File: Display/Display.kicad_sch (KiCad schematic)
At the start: 1 part, among them U1 74HC595

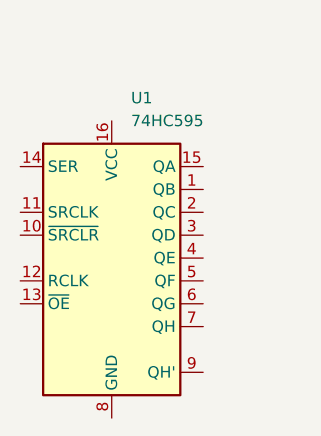
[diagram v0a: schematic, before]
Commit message: detach shift register
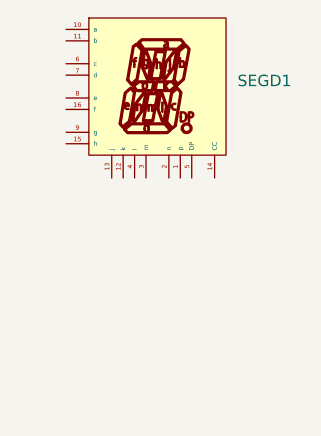
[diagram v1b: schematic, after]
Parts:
- removed U1: 74HC595, Package_SO:TSSOP-16_4.4x5mm_P0.65mm, symbol 74xx:74HC595
- added SEGD1: (no value), External_Parts:ACPSC04-41SEKWA, symbol External_Parts:ACPSC04-41SEKWA
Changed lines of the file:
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@@
 	(paper "A4")
 	(symbol
-		(lib_id "74xx:74HC595")
-		(at 82.55 72.39 0)
+		(lib_id "External_Parts:ACPSC04-41SEKWA")
+		(at 87.63 53.34 0)
 		(unit 1)
 		(exclude_from_sim no)
@@
 		(dnp no)
 		(fields_autoplaced yes)
-		(property "Reference" "U1"
-			(at 84.6933 54.61 0)
+		(property "Reference" "SEGD1"
+			(at 96.52 52.7049 0)
 			(effects
 				(font
@@
 			)
 		)
-		(property "Value" "74HC595"
-			(at 84.6933 57.15 0)
+		(property "Value" ""
+			(at 96.52 54.61 0)
 			(effects
 				(font
@@
 			)
 		)
-		(property "Footprint" "Package_SO:TSSOP-16_4.4x5mm_P0.65mm"
-			(at 82.55 72.39 0)
+		(property "Footprint" "External_Parts:ACPSC04-41SEKWA"
+			(at 87.63 53.34 0)
 			(effects
 				(font
@@
 			)
 		)
-		(property "Datasheet" "http://www.ti.com/lit/ds/symlink/sn74hc595.pdf"
-			(at 82.55 72.39 0)
+		(property "Datasheet" ""
+			(at 87.63 53.34 0)
 			(effects
 				(font
@@
 			)
 		)
-		(property "Description" "8-bit serial in/out Shift Register 3-State Outputs"
-			(at 82.55 72.39 0)
+		(property "Description" ""
+			(at 87.63 53.34 0)
 			(effects
 				(font
@@
 			)
 		)
-		(pin "14"
+		(pin "10"
+		)
+		(pin "11"
+		)
+		(pin "6"
+		)
+		(pin "7"
+		)
+		(pin "8"
+		)
+		(pin "16"
+		)
+		(pin "9"
+		)
+		(pin "15"
 		)
 		(pin "13"
-		)
-		(pin "10"
 		)
 		(pin "12"
@@
 		(pin "4"
 		)
-		(pin "5"
+		(pin "3"
 		)
-		(pin "6"
-		)
-		(pin "16"
-		)
-		(pin "11"
-		)
-		(pin "15"
+		(pin "2"
 		)
 		(pin "1"
 		)
-		(pin "2"
+		(pin "5"
 		)
-		(pin "3"
-		)
-		(pin "8"
-		)
-		(pin "7"
-		)
-		(pin "9"
+		(pin "14"
 		)
 		(instances
 			(project ""
 				(path "/4a3e89f9-ab44-4b68-b8a8-f6bfa5391fb1"
-					(reference "U1")
+					(reference "SEGD1")
 					(unit 1)
 				)

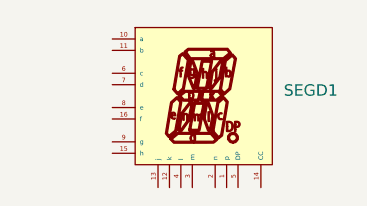
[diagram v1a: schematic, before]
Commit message: add chosen resistor
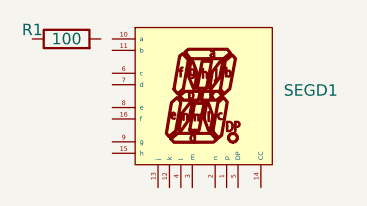
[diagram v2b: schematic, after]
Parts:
- added R1: 100, Resistor_SMD:R_0402_1005Metric_Pad0.72x0.64mm_HandSolder, symbol Device:R
- SEGD1: value (none) -> ~
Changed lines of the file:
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@@
 			)
 		)
-		(property "Value" ""
+		(property "Value" "~"
 			(at 96.52 54.61 0)
 			(effects
@@
 					(unit 1)
 				)
+			)
+		)
+	)
+	(symbol
+		(lib_id "Device:R")
+		(at 72.39 46.99 90)
+		(unit 1)
+		(exclude_from_sim no)
+		(in_bom yes)
+		(on_board yes)
+		(dnp no)
+		(property "Reference" "R1"
+			(at 68.58 45.974 90)
+			(effects
+				(font
+					(size 1.27 1.27)
+				)
+			)
+		)
+		(property "Value" "100"
+			(at 72.39 46.99 90)
+			(effects
+				(font
+					(size 1.27 1.27)
+				)
+			)
+		)
+		(property "Footprint" "Resistor_SMD:R_0402_1005Metric_Pad0.72x0.64mm_HandSolder"
+			(at 72.39 48.768 90)
+			(effects
+				(font
+					(size 1.27 1.27)
+				)
+				(hide yes)
+			)
+		)
+		(property "Datasheet" "https://jlcpcb.com/api/file/downloadByFileSystemAccessId/8579705907481001984"
+			(at 72.39 46.99 0)
+			(effects
+				(font
+					(size 1.27 1.27)
+				)
+				(hide yes)
+			)
+		)
+		(property "Description" "Resistor"
+			(at 72.39 46.99 0)
+			(effects
+				(font
+					(size 1.27 1.27)
+				)
+				(hide yes)
+			)
+		)
+		(property "LCSC" "C25076"
+			(at 72.39 46.99 90)
+			(effects
+				(font
+					(size 1.27 1.27)
+				)
+				(hide yes)
+			)
+		)
+		(pin "2"
+		)
+		(pin "1"
+		)
+		(instances
+			(project ""
+				(path "/4a3e89f9-ab44-4b68-b8a8-f6bfa5391fb1"
+					(reference "R1")
+					(unit 1)
+				)

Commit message: user save
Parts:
- added R10, R100, R101, R102, R103, R104, R105, R106, R107, R108, R109, R11, R110, R111, R112, R113, R114, R115, R116, R117, R118, R119, R12, R120, R121, R122, R123, R124, R125, R126, R127, R128, R129, R13, R130, R131, R132, R133, R134, R135, R136, R137, R138, R139, R14, R140, R141, R142, R143, R144, R145, R146, R147, R148, R149, R15, R150, R151, R152, R153, R154, R155, R156, R157, R158, R159, R16, R160, R161, R162, R163, R164, R165, R166, R167, R168, R169, R17, R170, R171, R172, R173, R174, R175, R176, R177, R178, R179, R18, R180, R181, R182, R183, R184, R185, R186, R187, R188, R189, R19, R190, R191, R192, R193, R194, R195, R196, R197, R198, R199, R2, R20, R200, R201, R202, R203, R204, R205, R206, R207, R208, R209, R21, R210, R211, R212, R213, R214, R215, R216, R217, R218, R219, R22, R220, R221, R222, R223, R224, R225, R226, R227, R228, R229, R23, R230, R231, R232, R233, R234, R235, R236, R237, R238, R239, R24, R240, R241, R242, R243, R244, R245, R246, R247, R248, R249, R25, R250, R251, R252, R253, R254, R255, R256, R257, R258, R259, R26, R260, R261, R262, R263, R264, R265, R266, R267, R268, R269, R27, R270, R271, R272, R273, R274, R275, R276, R277, R278, R279, R28, R280, R281, R282, R283, R284, R285, R286, R287, R288, R289, R29, R290, R291, R292, R293, R294, R295, R296, R297, R298, R299, R3, R30, R300, R301, R302, R303, R304, R305, R306, R307, R308, R309, R31, R310, R311, R312, R313, R314, R315, R316, R317, R318, R319, R32, R320, R321, R322, R323, R324, R325, R326, R327, R328, R329, R33, R330, R331, R332, R333, R334, R335, R336, R337, R338, R339, R34, R340, R341, R342, R343, R344, R345, R346, R347, R348, R349, R35, R350, R351, R352, R353, R354, R355, R356, R357, R358, R359, R36, R360, R361, R362, R363, R364, R365, R366, R367, R368, R369, R37, R370, R371, R372, R373, R374, R375, R376, R377, R378, R379, R38, R380, R381, R382, R383, R384, R385, R386, R387, R388, R389, R39, R390, R391, R392, R393, R394, R395, R396, R397, R398, R399, R4, R40, R400, R401, R402, R403, R404, R405, R406, R407, R408, R409, R41, R410, R411, R412, R413, R414, R415, R416, R417, R418, R419, R42, R420, R421, R422, R423, R424, R425, R426, R427, R428, R429, R43, R430, R431, R432, R433, R434, R435, R436, R437, R438, R439, R44, R440, R441, R442, R443, R444, R445, R446, R447, R448, R449, R45, R450, R451, R452, R453, R454, R455, R456, R457, R458, R459, R46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: 100, Resistor_SMD:R_0402_1005Metric_Pad0.72x0.64mm_HandSolder, symbol Device:R
- added SEGD2, SEGD3, SEGD4, SEGD5: ~, External_Parts:ACPSC04-41SEKWA, symbol External_Parts:ACPSC04-41SEKWA
- added U1, U10, U11, U12, U13, U14, U15, U16, U17, U18, U19, U2, U20, U21, U22, U23, U24, U25, U26, U27, U28, U29, U3, U30, U31, U32, U33, U34, U35, U36, U37, U38, U39, U4, U40, U41, U42, U43, U44, U45, U46, U47, U48, U49, U5, U50, U51, U52, U53, U54, U55, U56, U57, U58, U59, U6, U60, U61, U62, U63, U64, U65, U66, U67, U68, U69, U7, U70, U8, U9: 74HC595, Package_SO:TSSOP-16_4.4x5mm_P0.65mm, symbol 74xx:74HC595
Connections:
- net at SEGD1.1 (p): now also R14.2
- net at SEGD1.10 (a): now also R1.2
- net at SEGD1.11 (b): now also R2.2
- net at SEGD1.12 (k): now also R10.2
- net at SEGD1.13 (j): now also R9.2
- net GNDD: now reaches SEGD1.14 (CC)
- net GNDD: now also SEGD2.14 (CC), SEGD3.14 (CC), SEGD4.14 (CC), SEGD5.14 (CC), U1.8 (GND), U10.8 (GND), U11.8 (GND), U12.8 (GND), U13.8 (GND), U14.8 (GND), U15.8 (GND), U16.8 (GND)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
- net at SEGD1.15 (h): now also R8.2
- net at SEGD1.16 (f): now also R6.2
- net at SEGD1.2 (n): now also R13.2
- net at SEGD1.3 (m): now also R12.2
- net at SEGD1.4 (l): now also R11.2
- net at SEGD1.5 (DP): now also R15.2
- net at SEGD1.6 (c): now also R3.2
- net at SEGD1.7 (d): now also R4.2
- net at SEGD1.8 (e): now also R5.2
- net at SEGD1.9 (g): now also R7.2
- net at R1.1: now also U1.15 (QA)
- new net: R72.1, U9.7 (QH)
- new net: R72.2, SEGD5.3 (m)
- new net: R126.1, U16.5 (QF)
- new net: R34.1, U5.1 (QB)
- new net: R33.1, U5.15 (QA)
- new net: R35.1, U5.2 (QC)
- new net: R36.1, U5.3 (QD)
- new net: R37.1, U5.4 (QE)
- new net: R38.1, U5.5 (QF)
- new net: R39.1, U5.6 (QG)
- new net: R40.1, U5.7 (QH)
- new net: R335.1, U42.6 (QG)
- new net: R112.1, U14.7 (QH)
- new net: R535.1, U67.6 (QG)
- new net: R282.1, U36.1 (QB)
- new net: R427.1, U54.2 (QC)
- new net: R174.1, U22.5 (QF)
- new net: R435.1, U55.2 (QC)
- new net: R527.1, U66.6 (QG)
- new net: R510.1, U64.5 (QF)
- new net: R76.1, U10.3 (QD)
- new net: R468.1, U59.3 (QD)
- new net: R178.1, U23.1 (QB)
- new net: R177.1, U23.15 (QA)
- new net: R179.1, U23.2 (QC)
- new net: R180.1, U23.3 (QD)
- new net: R181.1, U23.4 (QE)
- new net: R182.1, U23.5 (QF)
- new net: R183.1, U23.6 (QG)
- new net: R184.1, U23.7 (QH)
- new net: R474.1, U60.1 (QB)
- new net: R411.1, U52.2 (QC)
- new net: R59.1, U8.2 (QC)
- new net: R59.2, SEGD4.1 (p)
- new net: R461.1, U58.4 (QE)
- new net: R278.1, U35.5 (QF)
- new net: R194.1, U25.1 (QB)
- new net: R193.1, U25.15 (QA)
- new net: R195.1, U25.2 (QC)
- new net: R196.1, U25.3 (QD)
- new net: R197.1, U25.4 (QE)
- new net: R198.1, U25.5 (QF)
- new net: R199.1, U25.6 (QG)
- new net: R200.1, U25.7 (QH)
- new net: R397.1, U50.4 (QE)
- new net: R145.1, U19.15 (QA)
- new net: R300.1, U38.3 (QD)
- new net: R516.1, U65.3 (QD)
- new net: R543.1, U68.6 (QG)
- new net: R323.1, U41.2 (QC)
- new net: R286.1, U36.5 (QF)
- new net: R66.1, U9.1 (QB)
- new net: R66.2, SEGD5.16 (f)
- new net: R489.1, U62.15 (QA)
- new net: R192.1, U24.7 (QH)
- new net: R449.1, U57.15 (QA)
- new net: R331.1, U42.2 (QC)
- new net: R86.1, U11.5 (QF)
- new net: R549.1, U69.4 (QE)
- new net: R167.1, U21.6 (QG)
- new net: R553.1, U70.15 (QA)
- new net: R529.1, U67.15 (QA)
- new net: R82.1, U11.1 (QB)
- new net: R318.1, U40.5 (QF)
- new net: R356.1, U45.3 (QD)
- new net: R437.1, U55.4 (QE)
- new net: R324.1, U41.3 (QD)
- new net: R490.1, U62.1 (QB)
- new net: R400.1, U50.7 (QH)
- new net: R154.1, U20.1 (QB)
- new net: R46.2, SEGD4.10 (a)
- new net: R47.2, SEGD4.11 (b)
- new net: R55.2, SEGD4.12 (k)
- new net: R54.2, SEGD4.13 (j)
- new net: R53.2, SEGD4.15 (h)
- new net: R51.2, SEGD4.16 (f)
- new net: R58.2, SEGD4.2 (n)
- new net: R57.2, SEGD4.3 (m)
- new net: R56.2, SEGD4.4 (l)
- new net: R60.2, SEGD4.5 (DP)
- new net: R48.2, SEGD4.6 (c)
- new net: R49.2, SEGD4.7 (d)
- new net: R50.2, SEGD4.8 (e)
- new net: R52.2, SEGD4.9 (g)
- new net: R98.1, U13.1 (QB)
- new net: R97.1, U13.15 (QA)
- new net: R99.1, U13.2 (QC)
- new net: R100.1, U13.3 (QD)
- new net: R101.1, U13.4 (QE)
- new net: R102.1, U13.5 (QF)
- new net: R103.1, U13.6 (QG)
- new net: R104.1, U13.7 (QH)
- new net: R311.1, U39.6 (QG)
- new net: R338.1, U43.1 (QB)
- new net: R506.1, U64.1 (QB)
- new net: R505.1, U64.15 (QA)
- new net: R507.1, U64.2 (QC)
- new net: R508.1, U64.3 (QD)
- new net: R509.1, U64.4 (QE)
- new net: R511.1, U64.6 (QG)
- new net: R512.1, U64.7 (QH)
- new net: R105.1, U14.15 (QA)
- new net: R367.1, U46.6 (QG)
- new net: R62.1, U8.5 (QF)
- new net: R62.2, SEGD5.11 (b)
- new net: R67.1, U9.2 (QC)
- new net: R67.2, SEGD5.9 (g)
- new net: R425.1, U54.15 (QA)
- new net: R550.1, U69.5 (QF)
- new net: R548.1, U69.3 (QD)
- new net: R519.1, U65.6 (QG)
- new net: R63.1, U8.6 (QG)
- new net: R63.2, SEGD5.6 (c)
- new net: R537.1, U68.15 (QA)
- new net: R348.1, U44.3 (QD)
- new net: R185.1, U24.15 (QA)
- new net: R269.1, U34.4 (QE)
- new net: R405.1, U51.4 (QE)
- new net: R117.1, U15.4 (QE)
- new net: R222.1, U28.5 (QF)
- new net: R423.1, U53.6 (QG)
- new net: R149.1, U19.4 (QE)
- new net: R551.1, U69.6 (QG)
- new net: R5.1, U1.4 (QE)
- new net: R131.1, U17.2 (QC)
- new net: R33.2, SEGD3.6 (c)
- new net: R221.1, U28.4 (QE)
- new net: R68.1, U9.3 (QD)
- new net: R68.2, SEGD5.15 (h)
- new net: R32.1, U4.7 (QH)
- new net: R32.2, SEGD3.11 (b)
- new net: R290.1, U37.1 (QB)
- new net: R254.1, U32.5 (QF)
- new net: R189.1, U24.4 (QE)
- new net: R339.1, U43.2 (QC)
- new net: R436.1, U55.3 (QD)
- new net: R471.1, U59.6 (QG)
- new net: R123.1, U16.2 (QC)
- new net: R283.1, U36.2 (QC)
- new net: R442.1, U56.1 (QB)
- new net: R299.1, U38.2 (QC)
- new net: R85.1, U11.4 (QE)
- new net: R233.1, U30.15 (QA)
- new net: R136.1, U17.7 (QH)
- new net: R354.1, U45.1 (QB)
- new net: R353.1, U45.15 (QA)
- new net: R355.1, U45.2 (QC)
- new net: R357.1, U45.4 (QE)
- new net: R358.1, U45.5 (QF)
- new net: R359.1, U45.6 (QG)
- new net: R360.1, U45.7 (QH)
- new net: R89.1, U12.15 (QA)
- new net: R94.1, U12.5 (QF)
- new net: R308.1, U39.3 (QD)
- new net: R457.1, U58.15 (QA)
- new net: R464.1, U58.7 (QH)
- new net: R499.1, U63.2 (QC)
- new net: R448.1, U56.7 (QH)
- new net: R191.1, U24.6 (QG)
- new net: R234.1, U30.1 (QB)
- new net: R113.1, U15.15 (QA)
- new net: R34.2, SEGD3.7 (d)
- new net: R284.1, U36.3 (QD)
- new net: R334.1, U42.5 (QF)
- new net: R110.1, U14.5 (QF)
- new net: R540.1, U68.3 (QD)
- new net: R202.1, U26.1 (QB)
- new net: R205.1, U26.4 (QE)
- new net: R71.1, U9.6 (QG)
- new net: R71.2, SEGD5.4 (l)
- new net: R394.1, U50.1 (QB)
- new net: R393.1, U50.15 (QA)
- new net: R395.1, U50.2 (QC)
- new net: R396.1, U50.3 (QD)
- new net: R398.1, U50.5 (QF)
- new net: R399.1, U50.6 (QG)
- new net: R559.1, U70.6 (QG)
- new net: R350.1, U44.5 (QF)
- new net: R230.1, U29.5 (QF)
- new net: R132.1, U17.3 (QD)
- new net: R143.1, U18.6 (QG)
- new net: R249.1, U32.15 (QA)
- new net: R115.1, U15.2 (QC)
- new net: R227.1, U29.2 (QC)
- new net: R554.1, U70.1 (QB)
- new net: R87.1, U11.6 (QG)
- new net: R558.1, U70.5 (QF)
- new net: R410.1, U52.1 (QB)
- new net: R250.1, U32.1 (QB)
- new net: R251.1, U32.2 (QC)
- new net: R252.1, U32.3 (QD)
- new net: R253.1, U32.4 (QE)
- new net: R255.1, U32.6 (QG)
- new net: R256.1, U32.7 (QH)
- new net: R50.1, U7.1 (QB)
- new net: R21.1, U3.4 (QE)
- new net: R21.2, SEGD2.16 (f)
- new net: R129.1, U17.15 (QA)
- new net: R153.1, U20.15 (QA)
- new net: R155.1, U20.2 (QC)
- new net: R156.1, U20.3 (QD)
- new net: R157.1, U20.4 (QE)
- new net: R158.1, U20.5 (QF)
- new net: R159.1, U20.6 (QG)
- new net: R160.1, U20.7 (QH)
- new net: R288.1, U36.7 (QH)
- new net: R469.1, U59.4 (QE)
- new net: R536.1, U67.7 (QH)
- new net: R201.1, U26.15 (QA)
- new net: R10.1, U2.1 (QB)
- new net: R170.1, U22.1 (QB)
- new net: R88.1, U11.7 (QH)
- new net: R7.1, U1.6 (QG)
- new net: R11.1, U2.2 (QC)
- new net: R210.1, U27.1 (QB)
- new net: R209.1, U27.15 (QA)
- new net: R211.1, U27.2 (QC)
- new net: R212.1, U27.3 (QD)
- new net: R213.1, U27.4 (QE)
- new net: R214.1, U27.5 (QF)
- new net: R215.1, U27.6 (QG)
- new net: R216.1, U27.7 (QH)
- new net: R362.1, U46.1 (QB)
- new net: R361.1, U46.15 (QA)
- new net: R363.1, U46.2 (QC)
- new net: R364.1, U46.3 (QD)
- new net: R365.1, U46.4 (QE)
- new net: R366.1, U46.5 (QF)
- new net: R368.1, U46.7 (QH)
- new net: R18.1, U3.1 (QB)
- new net: R17.1, U3.15 (QA)
- new net: R19.1, U3.2 (QC)
- new net: R20.1, U3.3 (QD)
- new net: R22.1, U3.5 (QF)
- new net: R23.1, U3.6 (QG)
- new net: R24.1, U3.7 (QH)
- new net: R138.1, U18.1 (QB)
- new net: R426.1, U54.1 (QB)
- new net: R428.1, U54.3 (QD)
- new net: R429.1, U54.4 (QE)
- new net: R430.1, U54.5 (QF)
- new net: R431.1, U54.6 (QG)
- new net: R432.1, U54.7 (QH)
- new net: R44.1, U6.3 (QD)
- new net: R44.2, SEGD3.1 (p)
- new net: R289.1, U37.15 (QA)
- new net: R139.1, U18.2 (QC)
- new net: R458.1, U58.1 (QB)
- new net: R459.1, U58.2 (QC)
- new net: R460.1, U58.3 (QD)
- new net: R462.1, U58.5 (QF)
- new net: R463.1, U58.6 (QG)
- new net: R203.1, U26.2 (QC)
- new net: R275.1, U35.2 (QC)
- new net: R75.1, U10.2 (QC)
- new net: R75.2, SEGD5.5 (DP)
- new net: R491.1, U62.2 (QC)
- new net: R492.1, U62.3 (QD)
- new net: R493.1, U62.4 (QE)
- new net: R494.1, U62.5 (QF)
- new net: R495.1, U62.6 (QG)
- new net: R496.1, U62.7 (QH)
- new net: R503.1, U63.6 (QG)
- new net: R130.1, U17.1 (QB)
- new net: R133.1, U17.4 (QE)
- new net: R134.1, U17.5 (QF)
- new net: R135.1, U17.6 (QG)
- new net: R271.1, U34.6 (QG)
- new net: R281.1, U36.15 (QA)
- new net: R298.1, U38.1 (QB)
- new net: R297.1, U38.15 (QA)
- new net: R301.1, U38.4 (QE)
- new net: R302.1, U38.5 (QF)
- new net: R303.1, U38.6 (QG)
- new net: R304.1, U38.7 (QH)
- new net: R241.1, U31.15 (QA)
- new net: R141.1, U18.4 (QE)
- new net: R420.1, U53.3 (QD)
- new net: R18.2, SEGD2.6 (c)
- new net: R330.1, U42.1 (QB)
- new net: R485.1, U61.4 (QE)
- new net: R165.1, U21.4 (QE)
- new net: R13.1, U2.4 (QE)
- new net: R47.1, U6.6 (QG)
- new net: R95.1, U12.6 (QG)
- new net: R451.1, U57.2 (QC)
- new net: R261.1, U33.4 (QE)
- new net: R41.1, U6.15 (QA)
- new net: R41.2, SEGD3.4 (l)
- new net: R258.1, U33.1 (QB)
- new net: R257.1, U33.15 (QA)
- new net: R259.1, U33.2 (QC)
- new net: R260.1, U33.3 (QD)
- new net: R262.1, U33.5 (QF)
- new net: R263.1, U33.6 (QG)
- new net: R264.1, U33.7 (QH)
- new net: R73.1, U10.15 (QA)
- new net: R73.2, SEGD5.2 (n)
- new net: R291.1, U37.2 (QC)
- new net: R443.1, U56.2 (QC)
- new net: R124.1, U16.3 (QD)
- new net: R273.1, U35.15 (QA)
- new net: R240.1, U30.7 (QH)
- new net: R369.1, U47.15 (QA)
- new net: R347.1, U44.2 (QC)
- new net: R218.1, U28.1 (QB)
- new net: R337.1, U43.15 (QA)
- new net: R340.1, U43.3 (QD)
- new net: R341.1, U43.4 (QE)
- new net: R342.1, U43.5 (QF)
- new net: R343.1, U43.6 (QG)
- new net: R344.1, U43.7 (QH)
- new net: R27.1, U4.2 (QC)
- new net: R27.2, SEGD2.3 (m)
- new net: R433.1, U55.15 (QA)
- new net: R310.1, U39.5 (QF)
- new net: R556.1, U70.3 (QD)
- new net: R237.1, U30.4 (QE)
- new net: R440.1, U55.7 (QH)
- new net: R169.1, U22.15 (QA)
- new net: R292.1, U37.3 (QD)
- new net: R530.1, U67.1 (QB)
- new net: R244.1, U31.3 (QD)
- new net: R274.1, U35.1 (QB)
- new net: R276.1, U35.3 (QD)
- new net: R277.1, U35.4 (QE)
- new net: R279.1, U35.6 (QG)
- new net: R280.1, U35.7 (QH)
- new net: R285.1, U36.4 (QE)
- new net: R54.1, U7.5 (QF)
- new net: R417.1, U53.15 (QA)
- new net: R38.2, SEGD3.15 (h)
- new net: R329.1, U42.15 (QA)
- new net: R332.1, U42.3 (QD)
- new net: R333.1, U42.4 (QE)
- new net: R336.1, U42.7 (QH)
- new net: R488.1, U61.7 (QH)
- new net: R486.1, U61.5 (QF)
- new net: R26.1, U4.1 (QB)
- new net: R26.2, SEGD2.4 (l)
- new net: R415.1, U52.6 (QG)
- new net: R452.1, U57.3 (QD)
- new net: R293.1, U37.4 (QE)
- new net: R501.1, U63.4 (QE)
- new net: R245.1, U31.4 (QE)
- new net: R150.1, U19.5 (QF)
- new net: R20.2, SEGD2.8 (e)
- new net: R31.2, SEGD3.10 (a)
- new net: R40.2, SEGD3.12 (k)
- new net: R39.2, SEGD3.13 (j)
- new net: R36.2, SEGD3.16 (f)
- new net: R43.2, SEGD3.2 (n)
- new net: R42.2, SEGD3.3 (m)
- new net: R45.2, SEGD3.5 (DP)
- new net: R35.2, SEGD3.8 (e)
- new net: R37.2, SEGD3.9 (g)
- new net: R60.1, U8.3 (QD)
- new net: R111.1, U14.6 (QG)
- new net: R219.1, U28.2 (QC)
- new net: R28.1, U4.3 (QD)
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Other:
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
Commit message: user save. too many dispalys
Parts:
- added SEGD10, SEGD11, SEGD12, SEGD13, SEGD14, SEGD15, SEGD16, SEGD17, SEGD18, SEGD19, SEGD20, SEGD21, SEGD22, SEGD23, SEGD24, SEGD25, SEGD26, SEGD27, SEGD28, SEGD29, SEGD30, SEGD31, SEGD32, SEGD33, SEGD34, SEGD35, SEGD36, SEGD37, SEGD6, SEGD7, SEGD8, SEGD9: ~, External_Parts:ACPSC04-41SEKWA, symbol External_Parts:ACPSC04-41SEKWA
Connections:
- net GNDD: now also SEGD10.14 (CC), SEGD11.14 (CC), SEGD12.14 (CC), SEGD13.14 (CC), SEGD14.14 (CC), SEGD15.14 (CC), SEGD16.14 (CC), SEGD17.14 (CC), SEGD18.14 (CC), SEGD19.14 (CC), SEGD20.14 (CC), SEGD21.14 (CC)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
- net at R126.2: now also SEGD9.16 (f)
- net at R335.2: now also SEGD23.8 (e)
- net at R112.2: now also SEGD8.9 (g)
- net at R535.2: now also SEGD36.12 (k)
- net at R282.2: now also SEGD19.3 (m)
- net at R427.2: now also SEGD29.9 (g)
- net at R174.2: now also SEGD12.13 (j)
- net at R435.2: now also SEGD29.5 (DP)
- net at R527.2: now also SEGD36.11 (b)
- net at R510.2: now also SEGD34.5 (DP)
- net CarryOverA0: now reaches R76.2
- net CarryOverA0: now also SEGD6.10 (a)
- net at R468.2: now also SEGD32.6 (c)
- net at R474.2: now also SEGD32.13 (j)
- net at R411.2: now also SEGD28.16 (f)
- net at R461.2: now also SEGD31.4 (l)
- net at R278.2: now also SEGD19.15 (h)
- net at R397.2: now also SEGD27.9 (g)
- net at R145.2: now also SEGD10.12 (k)
- net at R300.2: now also SEGD20.5 (DP)
- net at R516.2: now also SEGD35.16 (f)
- net at R543.2: now also SEGD37.6 (c)
- net at R323.2: now also SEGD22.15 (h)
- net at R177.2: now also SEGD12.3 (m)
- net at R286.2: now also SEGD20.10 (a)
- net at R489.2: now also SEGD33.13 (j)
- net at R192.2: now also SEGD13.3 (m)
- net at R449.2: now also SEGD30.1 (p)
- net at R331.2: now also SEGD23.10 (a)
- net at R86.2: now also SEGD6.4 (l)
- net at R549.2: now also SEGD37.13 (j)
- net at R167.2: now also SEGD12.11 (b)
- net at R529.2: now also SEGD36.7 (d)
- net at R82.2: now also SEGD6.9 (g)
- net CarryOverC2: now reaches R318.2
- net CarryOverC2: now also SEGD22.6 (c)
- net at R356.2: now also SEGD24.4 (l)
- net at R437.2: now also SEGD30.11 (b)
- net at R324.2: now also SEGD22.13 (j)
- net at R490.2: now also SEGD33.12 (k)
- net at R400.2: now also SEGD27.12 (k)
- net at R154.2: now also SEGD11.7 (d)
- net at R311.2: now also SEGD21.4 (l)
- net at R338.2: now also SEGD23.15 (h)
- net at R105.2: now also SEGD7.5 (DP)
- net at R367.2: now also SEGD25.9 (g)
- net at R425.2: now also SEGD29.8 (e)
- net at R550.2: now also SEGD37.12 (k)
- net at R548.2: now also SEGD37.15 (h)
- net at R519.2: now also SEGD35.13 (j)
- net at R537.2: now also SEGD36.3 (m)
- net at R348.2: now also SEGD24.6 (c)
- net at R185.2: now also SEGD13.8 (e)
- net at R269.2: now also SEGD18.1 (p)
- net CarryOverD4: now reaches R405.2
- net CarryOverD4: now also SEGD27.5 (DP)
- net at R117.2: now also SEGD8.3 (m)
- net at R222.2: now also SEGD15.3 (m)
- net at R423.2: now also SEGD29.6 (c)
- net at R184.2: now also SEGD13.7 (d)
- net at R149.2: now also SEGD10.1 (p)
- net at R551.2: now also SEGD37.4 (l)
- net at R131.2: now also SEGD9.4 (l)
- net at R221.2: now also SEGD15.4 (l)
- net at R290.2: now also SEGD20.8 (e)
- net at R254.2: now also SEGD17.1 (p)
- net at R189.2: now also SEGD13.13 (j)
- net at R339.2: now also SEGD23.13 (j)
- net at R436.2: now also SEGD30.10 (a)
- net at R471.2: now also SEGD32.16 (f)
- net at R123.2: now also SEGD9.6 (c)
- net at R283.2: now also SEGD19.2 (n)
- net at R442.2: now also SEGD30.9 (g)
- net at R299.2: now also SEGD20.1 (p)
- net at R85.2: now also SEGD6.12 (k)
- net at R233.2: now also SEGD16.15 (h)
- net at R136.2: now also SEGD10.10 (a)
- net at R97.2: now also SEGD7.9 (g)
- net at R103.2: now also SEGD7.2 (n)
- net at R183.2: now also SEGD13.6 (c)
- net at R89.2: now also SEGD6.1 (p)
- net at R94.2: now also SEGD7.7 (d)
- net at R308.2: now also SEGD21.15 (h)
- net at R457.2: now also SEGD31.9 (g)
- net at R464.2: now also SEGD31.1 (p)
- net at R499.2: now also SEGD34.7 (d)
- net at R448.2: now also SEGD30.2 (n)
- net at R191.2: now also SEGD13.4 (l)
- net at R234.2: now also SEGD16.13 (j)
- net at R113.2: now also SEGD8.15 (h)
- net at R284.2: now also SEGD19.1 (p)
- net at R334.2: now also SEGD23.7 (d)
- net at R110.2: now also SEGD8.8 (e)
- net at R540.2: now also SEGD36.5 (DP)
- net at R202.2: now also SEGD14.9 (g)
- net at R205.2: now also SEGD14.12 (k)
- net at R350.2: now also SEGD24.8 (e)
- net at R230.2: now also SEGD16.8 (e)
- net at R132.2: now also SEGD9.3 (m)
- net at R143.2: now also SEGD10.15 (h)
- net at R249.2: now also SEGD17.13 (j)
- net at R115.2: now also SEGD8.12 (k)
- net at R506.2: now also SEGD34.4 (l)
- net at R227.2: now also SEGD16.11 (b)
- net at R87.2: now also SEGD6.3 (m)
- net at R410.2: now also SEGD28.8 (e)
- net at R129.2: now also SEGD9.13 (j)
- net at R288.2: now also SEGD20.6 (c)
- net at R469.2: now also SEGD32.7 (d)
- net at R536.2: now also SEGD36.4 (l)
- net at R201.2: now also SEGD14.16 (f)
- net at R170.2: now also SEGD12.8 (e)
- net at R88.2: now also SEGD6.2 (n)
- net at R138.2: now also SEGD10.6 (c)
- net at R289.2: now also SEGD20.7 (d)
- net at R139.2: now also SEGD10.7 (d)
- net at R203.2: now also SEGD14.15 (h)
- net at R275.2: now also SEGD19.8 (e)
- net at R503.2: now also SEGD34.15 (h)
- net at R271.2: now also SEGD19.10 (a)
- net at R281.2: now also SEGD19.4 (l)
- net at R214.2: now also SEGD15.7 (d)
- net at R241.2: now also SEGD17.10 (a)
- net at R141.2: now also SEGD10.16 (f)
- net at R420.2: now also SEGD28.5 (DP)
- net at R200.2: now also SEGD14.8 (e)
- net at R330.2: now also SEGD22.5 (DP)
- net at R485.2: now also SEGD33.8 (e)
- net CarryOverB4: now reaches R165.2
- net CarryOverB4: now also SEGD11.5 (DP)
- net at R250.2: now also SEGD17.12 (k)
- net at R95.2: now also SEGD7.8 (e)
- net at R393.2: now also SEGD27.6 (c)
- net at R451.2: now also SEGD31.10 (a)
- net at R462.2: now also SEGD31.3 (m)
- net at R261.2: now also SEGD18.16 (f)
- net at R511.2: now also SEGD35.10 (a)
- net at R291.2: now also SEGD20.16 (f)
- net at R443.2: now also SEGD30.15 (h)
- net at R124.2: now also SEGD9.7 (d)
- net at R273.2: now also SEGD19.6 (c)
- net at R240.2: now also SEGD16.5 (DP)
- net at R369.2: now also SEGD25.13 (j)
- net at R255.2: now also SEGD17.5 (DP)
- net at R507.2: now also SEGD34.3 (m)
- net at R347.2: now also SEGD24.11 (b)
- net at R218.2: now also SEGD15.15 (h)
- net at R252.2: now also SEGD17.3 (m)
- net at R302.2: now also SEGD21.11 (b)
- net at R432.2: now also SEGD29.3 (m)
- net at R433.2: now also SEGD29.2 (n)
- net at R310.2: now also SEGD21.12 (k)
- net at R237.2: now also SEGD16.3 (m)
- net at R494.2: now also SEGD33.1 (p)
- net at R440.2: now also SEGD30.8 (e)
- net at R496.2: now also SEGD34.10 (a)
- net at R169.2: now also SEGD12.7 (d)
- net at R258.2: now also SEGD18.6 (c)
- net at R292.2: now also SEGD20.9 (g)
- net at R530.2: now also SEGD36.8 (e)
- net at R212.2: now also SEGD15.11 (b)
- net at R244.2: now also SEGD17.7 (d)
- net at R260.2: now also SEGD18.8 (e)
- net at R159.2: now also SEGD11.13 (j)
- net at R199.2: now also SEGD14.7 (d)
- net at R363.2: now also SEGD25.6 (c)
- net at R285.2: now also SEGD19.5 (DP)
- net at R417.2: now also SEGD28.3 (m)
- net at R196.2: now also SEGD14.10 (a)
- net at R488.2: now also SEGD33.15 (h)
- net at R486.2: now also SEGD33.16 (f)
- net at R398.2: now also SEGD27.15 (h)
- net at R415.2: now also SEGD28.12 (k)
- net at R452.2: now also SEGD31.11 (b)
- net at R301.2: now also SEGD21.10 (a)
- net at R102.2: now also SEGD7.3 (m)
- net at R394.2: now also SEGD27.7 (d)
- net at R293.2: now also SEGD20.15 (h)
- net at R501.2: now also SEGD34.16 (f)
- net at R304.2: now also SEGD21.7 (d)
- net at R365.2: now also SEGD25.8 (e)
- net at R245.2: now also SEGD17.8 (e)
- net at R150.2: now also SEGD10.5 (DP)
- net at R463.2: now also SEGD31.2 (n)
- net at R98.2: now also SEGD7.15 (h)
- net at R111.2: now also SEGD8.16 (f)
- net at R219.2: now also SEGD15.13 (j)
- net at R355.2: now also SEGD24.12 (k)
- net at R498.2: now also SEGD34.6 (c)
- net at R534.2: now also SEGD36.13 (j)
- net at R322.2: now also SEGD22.9 (g)
- net at R473.2: now also SEGD32.15 (h)
- net CarryOverA4: now reaches R80.2
- net CarryOverA4: now also SEGD6.8 (e)
- net at R364.2: now also SEGD25.7 (d)
- net at R505.2: now also SEGD34.12 (k)
- net at R458.2: now also SEGD31.15 (h)
- net at R399.2: now also SEGD27.13 (j)
- net at R361.2: now also SEGD25.10 (a)
- net at R168.2: now also SEGD12.6 (c)
- net at R93.2: now also SEGD7.6 (c)
- net at R456.2: now also SEGD31.16 (f)
- net at R351.2: now also SEGD24.16 (f)
- net at R84.2: now also SEGD6.13 (j)
- net at R376.2: now also SEGD26.10 (a)
- net at R157.2: now also SEGD11.9 (g)
- net at R238.2: now also SEGD16.2 (n)
- net at R480.2: now also SEGD32.5 (DP)
- net at R294.2: now also SEGD20.13 (j)
- net at R128.2: now also SEGD9.15 (h)
- net at R438.2: now also SEGD30.6 (c)
- net at R345.2: now also SEGD23.5 (DP)
- net at R96.2: now also SEGD7.16 (f)
- net at R321.2: now also SEGD22.16 (f)
- net at R359.2: now also SEGD24.1 (p)
- net at R460.2: now also SEGD31.12 (k)
- net at R478.2: now also SEGD32.2 (n)
- net at R497.2: now also SEGD34.11 (b)
- net at R187.2: now also SEGD13.9 (g)
- net at R235.2: now also SEGD16.12 (k)
- net at R368.2: now also SEGD25.15 (h)
- net at R413.2: now also SEGD28.15 (h)
- net at R541.2: now also SEGD37.10 (a)
- net at R387.2: now also SEGD26.3 (m)
- net at R253.2: now also SEGD17.2 (n)
- net at R104.2: now also SEGD7.1 (p)
- net at R484.2: now also SEGD33.7 (d)
- net at R381.2: now also SEGD26.16 (f)
- net at R418.2: now also SEGD28.2 (n)
- net at R127.2: now also SEGD9.9 (g)
- net at R236.2: now also SEGD16.4 (l)
- net at R342.2: now also SEGD23.3 (m)
- net at R539.2: now also SEGD36.1 (p)
- net CarryOverB2: now reaches R163.2
- net CarryOverB2: now also SEGD11.2 (n)
- net at R314.2: now also SEGD21.1 (p)
- net at R483.2: now also SEGD33.6 (c)
- net CarryOverC3: now reaches R319.2
- net CarryOverC3: now also SEGD22.7 (d)
- net at R247.2: now also SEGD17.9 (g)
- net at R383.2: now also SEGD26.15 (h)
- net at R414.2: now also SEGD28.13 (j)
- net at R522.2: now also SEGD35.3 (m)
- net at R270.2: now also SEGD18.5 (DP)
- net at R513.2: now also SEGD35.6 (c)
- net at R251.2: now also SEGD17.4 (l)
- net at R492.2: now also SEGD33.3 (m)
- net at R467.2: now also SEGD32.11 (b)
- net at R309.2: now also SEGD21.13 (j)
- net at R118.2: now also SEGD8.2 (n)
- net at R382.2: now also SEGD26.9 (g)
- net at R99.2: now also SEGD7.13 (j)
- net at R262.2: now also SEGD18.9 (g)
- net at R91.2: now also SEGD7.10 (a)
- net at R336.2: now also SEGD23.16 (f)
- net at R173.2: now also SEGD12.15 (h)
- net CarryOverA1: now reaches R77.2
- net CarryOverA1: now also SEGD6.11 (b)
- net at R482.2: now also SEGD33.11 (b)
- net at R223.2: now also SEGD15.2 (n)
- net at R329.2: now also SEGD22.1 (p)
- net at R526.2: now also SEGD36.10 (a)
- net at R231.2: now also SEGD16.16 (f)
- net at R358.2: now also SEGD24.2 (n)
- net at R396.2: now also SEGD27.16 (f)
- net at R109.2: now also SEGD8.7 (d)
- net at R274.2: now also SEGD19.7 (d)
- net at R542.2: now also SEGD37.11 (b)
- net at R353.2: now also SEGD24.15 (h)
- net at R521.2: now also SEGD35.4 (l)
- net at R226.2: now also SEGD16.10 (a)
- net at R119.2: now also SEGD8.1 (p)
- net at R195.2: now also SEGD13.5 (DP)
- net at R100.2: now also SEGD7.12 (k)
- net at R545.2: now also SEGD37.8 (e)
- net at R454.2: now also SEGD31.7 (d)
- net at R206.2: now also SEGD14.4 (l)
- net at R306.2: now also SEGD21.16 (f)
- net at R312.2: now also SEGD21.3 (m)
- net at R280.2: now also SEGD19.12 (k)
- net at R120.2: now also SEGD8.5 (DP)
- net at R279.2: now also SEGD19.13 (j)
- net at R372.2: now also SEGD25.3 (m)
- net at R243.2: now also SEGD17.6 (c)
- net at R81.2: now also SEGD6.16 (f)
- net at R366.2: now also SEGD25.16 (f)
- net at R152.2: now also SEGD11.11 (b)
- net at R341.2: now also SEGD23.4 (l)
- net at R531.2: now also SEGD36.16 (f)
- net CarryOverC4: now reaches R320.2
- net CarryOverC4: now also SEGD22.8 (e)
- net at R538.2: now also SEGD36.2 (n)
- net at R130.2: now also SEGD9.12 (k)
- net at R332.2: now also SEGD23.11 (b)
- net at R186.2: now also SEGD13.16 (f)
- net at R188.2: now also SEGD13.15 (h)
- net CarryOverC1: now reaches R317.2
- net CarryOverC1: now also SEGD22.11 (b)
- net at R176.2: now also SEGD12.4 (l)
- net at R421.2: now also SEGD29.10 (a)
- net at R116.2: now also SEGD8.4 (l)
- net at R360.2: now also SEGD24.5 (DP)
- net CarryOverB3: now reaches R164.2
- net CarryOverB3: now also SEGD11.1 (p)
- net at R268.2: now also SEGD18.2 (n)
- net at R166.2: now also SEGD12.10 (a)
- net CarryOverA3: now reaches R79.2
- net CarryOverA3: now also SEGD6.7 (d)
- net at R198.2: now also SEGD14.6 (c)
- net at R133.2: now also SEGD9.2 (n)
- net at R248.2: now also SEGD17.15 (h)
- net at R228.2: now also SEGD16.6 (c)
- net at R272.2: now also SEGD19.11 (b)
- net at R408.2: now also SEGD28.6 (c)
- net at R326.2: now also SEGD22.4 (l)
- net at R533.2: now also SEGD36.15 (h)
- net at R518.2: now also SEGD35.15 (h)
- net at R491.2: now also SEGD33.4 (l)
- net at R137.2: now also SEGD10.11 (b)
- net at R395.2: now also SEGD27.8 (e)
- net at R495.2: now also SEGD33.5 (DP)
- net at R546.2: now also SEGD37.16 (f)
- net at R216.2: now also SEGD15.16 (f)
- net at R371.2: now also SEGD25.4 (l)
- net at R106.2: now also SEGD8.10 (a)
- net at R277.2: now also SEGD19.9 (g)
- net at R419.2: now also SEGD28.1 (p)
- net at R171.2: now also SEGD12.16 (f)
- net at R450.2: now also SEGD30.5 (DP)
- net at R377.2: now also SEGD26.11 (b)
- net at R101.2: now also SEGD7.4 (l)
- net at R92.2: now also SEGD7.11 (b)
- net CarryOverD1: now reaches R402.2
- net CarryOverD1: now also SEGD27.3 (m)
- net at R544.2: now also SEGD37.7 (d)
- net at R428.2: now also SEGD29.15 (h)
- net at R108.2: now also SEGD8.6 (c)
- net at R160.2: now also SEGD11.12 (k)
- net at R175.2: now also SEGD12.12 (k)
- net CarryOverD3: now reaches R404.2
- net CarryOverD3: now also SEGD27.1 (p)
- net at R406.2: now also SEGD28.10 (a)
- net at R148.2: now also SEGD10.2 (n)
- net at R354.2: now also SEGD24.13 (j)
- net at R422.2: now also SEGD29.11 (b)
- net at R142.2: now also SEGD10.9 (g)
- net at R287.2: now also SEGD20.11 (b)
- net at R466.2: now also SEGD32.10 (a)
- net at R409.2: now also SEGD28.7 (d)
- net CarryOverD0: now reaches R401.2
- net CarryOverD0: now also SEGD27.4 (l)
- net at R500.2: now also SEGD34.8 (e)
- net at R455.2: now also SEGD31.8 (e)
- net at R378.2: now also SEGD26.6 (c)
- net at R392.2: now also SEGD27.11 (b)
- net at R296.2: now also SEGD20.4 (l)
- net at R298.2: now also SEGD20.2 (n)
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
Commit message: user save
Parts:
- removed R425, R426, R427, R428, R429, R430, R431, R432, R433, R434, R435, R436, R437, R438, R439, R440, R441, R442, R443, R444, R445, R446, R447, R448, R449, R450, R451, R452, R453, R454, R455, R456, R457, R458, R459, R460, R461, R462, R463, R464, R465, R466, R467, R468, R469, R470, R471, R472, R473, R474, R475, R476, R477, R478, R479, R480, R481, R482, R483, R484, R485, R486, R487, R488, R489, R490, R491, R492, R493, R494, R495, R496, R497, R498, R499, R500, R501, R502, R503, R504, R505, R506, R507, R508, R509, R510, R511, R512, R513, R514, R515, R516, R517, R518, R519, R520, R521, R522, R523, R524, R525, R526, R527, R528, R529, R530, R531, R532, R533, R534, R535, R536, R537, R538, R539, R540, R541, R542, R543, R544, R545, R546, R547, R548, R549, R550, R551, R552, R553, R554, R555, R556, R557, R558, R559, R560: 100, Resistor_SMD:R_0402_1005Metric_Pad0.72x0.64mm_HandSolder, symbol Device:R
- removed SEGD29, SEGD30, SEGD31, SEGD32, SEGD33, SEGD34, SEGD35, SEGD36, SEGD37: ~, External_Parts:ACPSC04-41SEKWA, symbol External_Parts:ACPSC04-41SEKWA
- removed U54, U55, U56, U57, U58, U59, U60, U61, U62, U63, U64, U65, U66, U67, U68, U69, U70: 74HC595, Package_SO:TSSOP-16_4.4x5mm_P0.65mm, symbol 74xx:74HC595
- SEGD1: DigiKey (none) -> ACPSC04-41SEKWA
- U1: DigiKey (none) -> 74HC595PW,118
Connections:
- net SRCR: now reaches U5.10 (~{SRCLR})
- net SRCR: now also U1.10 (~{SRCLR}), U10.10 (~{SRCLR}), U11.10 (~{SRCLR}), U12.10 (~{SRCLR}), U13.10 (~{SRCLR}), U14.10 (~{SRCLR}), U15.10 (~{SRCLR}), U16.10 (~{SRCLR}), U17.10 (~{SRCLR}), U18.10 (~{SRCLR}), U19.10 (~{SRCLR}), U2.10 (~{SRCLR}), U20.10 (~{SRCLR}), U21.10 (~{SRCLR}), U22.10 (~{SRCLR}), U23.10 (~{SRCLR}), U24.10 (~{SRCLR}), U25.10 (~{SRCLR}), U26.10 (~{SRCLR}), U27.10 (~{SRCLR}), U28.10 (~{SRCLR}), U29.10 (~{SRCLR}), U3.10 (~{SRCLR}), U30.10 (~{SRCLR}), U31.10 (~{SRCLR}), U32.10 (~{SRCLR}), U33.10 (~{SRCLR}), U34.10 (~{SRCLR}), U35.10 (~{SRCLR}), U36.10 (~{SRCLR}), U37.10 (~{SRCLR}), U38.10 (~{SRCLR}), U39.10 (~{SRCLR}), U4.10 (~{SRCLR}), U40.10 (~{SRCLR}), U41.10 (~{SRCLR}), U42.10 (~{SRCLR}), U43.10 (~{SRCLR}), U44.10 (~{SRCLR}), U45.10 (~{SRCLR}), U46.10 (~{SRCLR}), U47.10 (~{SRCLR}), U48.10 (~{SRCLR}), U49.10 (~{SRCLR}), U50.10 (~{SRCLR}), U51.10 (~{SRCLR}), U52.10 (~{SRCLR}), U53.10 (~{SRCLR}), U6.10 (~{SRCLR}), U7.10 (~{SRCLR}), U8.10 (~{SRCLR}), U9.10 (~{SRCLR})
- net SRCL: now reaches U5.11 (SRCLK)
- net SRCL: now also U1.11 (SRCLK), U10.11 (SRCLK), U11.11 (SRCLK), U12.11 (SRCLK), U13.11 (SRCLK), U14.11 (SRCLK), U15.11 (SRCLK), U16.11 (SRCLK), U17.11 (SRCLK), U18.11 (SRCLK), U19.11 (SRCLK), U2.11 (SRCLK), U20.11 (SRCLK), U21.11 (SRCLK), U22.11 (SRCLK), U23.11 (SRCLK), U24.11 (SRCLK), U25.11 (SRCLK), U26.11 (SRCLK), U27.11 (SRCLK), U28.11 (SRCLK), U29.11 (SRCLK), U3.11 (SRCLK), U30.11 (SRCLK), U31.11 (SRCLK), U32.11 (SRCLK), U33.11 (SRCLK), U34.11 (SRCLK), U35.11 (SRCLK), U36.11 (SRCLK), U37.11 (SRCLK), U38.11 (SRCLK), U39.11 (SRCLK), U4.11 (SRCLK), U40.11 (SRCLK), U41.11 (SRCLK), U42.11 (SRCLK), U43.11 (SRCLK), U44.11 (SRCLK), U45.11 (SRCLK), U46.11 (SRCLK), U47.11 (SRCLK), U48.11 (SRCLK), U49.11 (SRCLK), U50.11 (SRCLK), U51.11 (SRCLK), U52.11 (SRCLK), U53.11 (SRCLK), U6.11 (SRCLK), U7.11 (SRCLK), U8.11 (SRCLK), U9.11 (SRCLK)
- net RCL: now reaches U5.12 (RCLK)
- net RCL: now also U1.12 (RCLK), U10.12 (RCLK), U11.12 (RCLK), U12.12 (RCLK), U13.12 (RCLK), U14.12 (RCLK), U15.12 (RCLK), U16.12 (RCLK), U17.12 (RCLK), U18.12 (RCLK), U19.12 (RCLK), U2.12 (RCLK), U20.12 (RCLK), U21.12 (RCLK), U22.12 (RCLK), U23.12 (RCLK), U24.12 (RCLK), U25.12 (RCLK), U26.12 (RCLK), U27.12 (RCLK), U28.12 (RCLK), U29.12 (RCLK), U3.12 (RCLK), U30.12 (RCLK), U31.12 (RCLK), U32.12 (RCLK), U33.12 (RCLK), U34.12 (RCLK), U35.12 (RCLK), U36.12 (RCLK), U37.12 (RCLK), U38.12 (RCLK), U39.12 (RCLK), U4.12 (RCLK), U40.12 (RCLK), U41.12 (RCLK), U42.12 (RCLK), U43.12 (RCLK), U44.12 (RCLK), U45.12 (RCLK), U46.12 (RCLK), U47.12 (RCLK), U48.12 (RCLK), U49.12 (RCLK), U50.12 (RCLK), U51.12 (RCLK), U52.12 (RCLK), U53.12 (RCLK), U6.12 (RCLK), U7.12 (RCLK), U8.12 (RCLK), U9.12 (RCLK)
- net ~{OE}: now reaches U5.13 (~{OE})
- net ~{OE}: now also U1.13 (~{OE}), U10.13 (~{OE}), U11.13 (~{OE}), U12.13 (~{OE}), U13.13 (~{OE}), U14.13 (~{OE}), U15.13 (~{OE}), U16.13 (~{OE}), U17.13 (~{OE}), U18.13 (~{OE}), U19.13 (~{OE}), U2.13 (~{OE}), U20.13 (~{OE}), U21.13 (~{OE}), U22.13 (~{OE}), U23.13 (~{OE}), U24.13 (~{OE}), U25.13 (~{OE}), U26.13 (~{OE}), U27.13 (~{OE}), U28.13 (~{OE}), U29.13 (~{OE}), U3.13 (~{OE}), U30.13 (~{OE}), U31.13 (~{OE}), U32.13 (~{OE}), U33.13 (~{OE}), U34.13 (~{OE}), U35.13 (~{OE}), U36.13 (~{OE}), U37.13 (~{OE}), U38.13 (~{OE}), U39.13 (~{OE}), U4.13 (~{OE}), U40.13 (~{OE}), U41.13 (~{OE}), U42.13 (~{OE}), U43.13 (~{OE}), U44.13 (~{OE}), U45.13 (~{OE}), U46.13 (~{OE}), U47.13 (~{OE}), U48.13 (~{OE}), U49.13 (~{OE}), U50.13 (~{OE}), U51.13 (~{OE}), U52.13 (~{OE}), U53.13 (~{OE}), U6.13 (~{OE}), U7.13 (~{OE}), U8.13 (~{OE}), U9.13 (~{OE})
- net at U5.14 (SER): now also U4.9 (QH')
- net at U5.9 (QH'): now also U6.14 (SER)
- net at U23.14 (SER): now also U22.9 (QH')
- net at U23.9 (QH'): now also U24.14 (SER)
- net at U25.14 (SER): now also U24.9 (QH')
- net at U25.9 (QH'): now also U26.14 (SER)
- net at U13.14 (SER): now also U12.9 (QH')
- net at U13.9 (QH'): now also U14.14 (SER)
- net at U45.14 (SER): now also U44.9 (QH')
- net at U45.9 (QH'): now also U46.14 (SER)
- net at U50.14 (SER): now also U49.9 (QH')
- net at U50.9 (QH'): now also U51.14 (SER)
- net at U32.14 (SER): now also U31.9 (QH')
- net at U32.9 (QH'): now also U33.14 (SER)
- net at U20.14 (SER): now also U19.9 (QH')
- net at U20.9 (QH'): now also U21.14 (SER)
- net at U27.14 (SER): now also U26.9 (QH')
- net at U27.9 (QH'): now also U28.14 (SER)
- net at U46.9 (QH'): now also U47.14 (SER)
- net at U3.14 (SER): now also U2.9 (QH')
- net at U3.9 (QH'): now also U4.14 (SER)
- net at U17.14 (SER): now also U16.9 (QH')
- net at U17.9 (QH'): now also U18.14 (SER)
- net at U38.14 (SER): now also U37.9 (QH')
- net at U38.9 (QH'): now also U39.14 (SER)
- net at U33.9 (QH'): now also U34.14 (SER)
- net at U43.14 (SER): now also U42.9 (QH')
- net at U43.9 (QH'): now also U44.14 (SER)
- net at U35.14 (SER): now also U34.9 (QH')
- net at U35.9 (QH'): now also U36.14 (SER)
- net at U42.14 (SER): now also U41.9 (QH')
- net at U28.9 (QH'): now also U29.14 (SER)
- net at U37.14 (SER): now also U36.9 (QH')
- net SR: now reaches U1.14 (SER)
- net at U1.9 (QH'): now also U2.14 (SER)
- net at U21.9 (QH'): now also U22.14 (SER)
- net at U10.14 (SER): now also U9.9 (QH')
- net at U10.9 (QH'): now also U11.14 (SER)
- net at U11.9 (QH'): now also U12.14 (SER)
- net at U31.14 (SER): now also U30.9 (QH')
- net at U41.14 (SER): now also U40.9 (QH')
- net at U30.14 (SER): now also U29.9 (QH')
- net at U7.14 (SER): now also U6.9 (QH')
- net at U7.9 (QH'): now also U8.14 (SER)
- net at U19.14 (SER): now also U18.9 (QH')
- net at U9.14 (SER): now also U8.9 (QH')
- net at U47.9 (QH'): now also U48.14 (SER)
- net at U40.14 (SER): now also U39.9 (QH')
- net at U53.14 (SER): now also U52.9 (QH')
- net at U49.14 (SER): now also U48.9 (QH')
- net at U14.9 (QH'): now also U15.14 (SER)
- net at U51.9 (QH'): now also U52.14 (SER)
- net at U15.9 (QH'): now also U16.14 (SER)
